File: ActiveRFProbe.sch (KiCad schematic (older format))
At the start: 41 parts, among them J1 Conn_01x01, J16 Conn_01x01, J17 Conn_01x01, J18 Conn_01x01, J19 Conn_01x01, J2 Conn_01x01, J20 Conn_01x01, J21 Conn_01x01, J22 Conn_01x01, J23 Conn_01x01, J24 Conn_01x01, J25 Conn_Coaxial, J3 Conn_01x01, Q1 2SC3357, Q2 2SC3357, Q3 2SC3357

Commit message: Fixed edge detector
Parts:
- removed C7: 10 nF, Capacitors_SMD:C_0805_HandSoldering, symbol C_Small
- added R13: 10k, Resistors_SMD:R_0805_HandSoldering, symbol R
- J25: footprint ActiveRFProbe:bnc_90_1-1337543-0_pad_combo -> ActiveRFProbe:Amphenol_RF_SMA_132289
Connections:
- net GND: now also R13.1
- net at C6.2, Q3.1 (E), R10.1: now also R9.2
- net at C8.2, D5.1 (K), J17.1 (Pin_1): now also R13.2
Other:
- moved on the sheet: D5, R9
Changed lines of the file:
@@
 L R R9
 U 1 1 5E9BA4DA
-P 6050 4450
-F 0 "R9" V 6130 4450 50  0000 C CNN
-F 1 "10k" V 6050 4450 50  0000 C CNN
-F 2 "Resistors_SMD:R_0805_HandSoldering" V 5980 4450 50  0001 C CNN
-F 3 "" H 6050 4450 50  0001 C CNN
-	1    6050 4450
+P 5850 4450
+F 0 "R9" V 5930 4450 50  0000 C CNN
+F 1 "10k" V 5850 4450 50  0000 C CNN
+F 2 "Resistors_SMD:R_0805_HandSoldering" V 5780 4450 50  0001 C CNN
+F 3 "" H 5850 4450 50  0001 C CNN
+	1    5850 4450
 	0    1    1    0
 $EndComp
@@
 $EndComp
 $Comp
-L C_Small C7
-U 1 1 5E9DAA86
-P 5800 4450
-F 0 "C7" H 5810 4520 50  0000 L CNN
-F 1 "10 nF" V 5650 4350 50  0000 L CNN
-F 2 "Capacitors_SMD:C_0805_HandSoldering" H 5800 4450 50  0001 C CNN
-F 3 "" H 5800 4450 50  0001 C CNN
-	1    5800 4450
-	0    1    1    0
-$EndComp
-$Comp
-L GND #PWR17
+L GND #PWR18
 U 1 1 5E9DC195
 P 6750 4950
-F 0 "#PWR17" H 6750 4700 50  0001 C CNN
+F 0 "#PWR18" H 6750 4700 50  0001 C CNN
 F 1 "GND" H 6750 4800 50  0000 C CNN
 F 2 "" H 6750 4950 50  0001 C CNN
@@
 F 0 "J25" H 6460 3870 50  0000 C CNN
 F 1 "Conn_Coaxial" V 6565 3750 50  0000 C CNN
-F 2 "ActiveRFProbe:bnc_90_1-1337543-0_pad_combo" H 6450 3750 50  0001 C CNN
+F 2 "ActiveRFProbe:Amphenol_RF_SMA_132289" H 6450 3750 50  0001 C CNN
 F 3 "" H 6450 3750 50  0001 C CNN
 	1    6450 3750
@@
 L D_Schottky D5
 U 1 1 5E9C8115
-P 6450 4450
-F 0 "D5" H 6450 4550 50  0000 C CNN
-F 1 "LRB751V" H 6450 4350 50  0000 C CNN
-F 2 "Diodes_SMD:D_SOD-323_HandSoldering" H 6450 4450 50  0001 C CNN
-F 3 "" H 6450 4450 50  0001 C CNN
-	1    6450 4450
-	-1   0    0    1
-$EndComp
-$Comp
-L GND #PWR18
+P 6200 4450
+F 0 "D5" H 6200 4550 50  0000 C CNN
+F 1 "LRB751V" H 6200 4350 50  0000 C CNN
+F 2 "Diodes_SMD:D_SOD-323_HandSoldering" H 6200 4450 50  0001 C CNN
+F 3 "" H 6200 4450 50  0001 C CNN
+	1    6200 4450
+	-1   0    0    1
+$EndComp
+$Comp
+L GND #PWR19
 U 1 1 5E9E423A
 P 7150 4950
-F 0 "#PWR18" H 7150 4700 50  0001 C CNN
+F 0 "#PWR19" H 7150 4700 50  0001 C CNN
 F 1 "GND" H 7150 4800 50  0000 C CNN
 F 2 "" H 7150 4950 50  0001 C CNN
@@
 Connection ~ 5700 4250
 Wire Wire Line
-	5900 4450 5900 4450
-Wire Wire Line
-	6600 4450 7150 4450
+	6350 4450 7150 4450
 Wire Wire Line
 	6750 4950 6750 4750
@@
 Wire Wire Line
 	3500 1800 3500 1900
-Wire Wire Line
-	6300 4450 6200 4450
 Wire Wire Line
 	7150 4950 7150 4700
@@
 	1    0    0    -1
 $EndComp
+$Comp
+L R R13
+U 1 1 5E9E674D
+P 6450 4650
+F 0 "R13" V 6530 4650 50  0000 C CNN
+F 1 "10k" V 6450 4650 50  0000 C CNN
+F 2 "Resistors_SMD:R_0805_HandSoldering" V 6380 4650 50  0001 C CNN
+F 3 "" H 6450 4650 50  0001 C CNN
+	1    6450 4650
+	-1   0    0    1
+$EndComp
+Wire Wire Line
+	6450 4500 6450 4450
+Connection ~ 6450 4450
+$Comp
+L GND #PWR17
+U 1 1 5E9E68D7
+P 6450 4950
+F 0 "#PWR17" H 6450 4700 50  0001 C CNN
+F 1 "GND" H 6450 4800 50  0000 C CNN
+F 2 "" H 6450 4950 50  0001 C CNN
+F 3 "" H 6450 4950 50  0001 C CNN
+	1    6450 4950
+	1    0    0    -1
+$EndComp
+Wire Wire Line
+	6450 4950 6450 4800
+Wire Wire Line
+	6050 4450 6000 4450
 $EndSCHEMATC

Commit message: Cleaned up the layout
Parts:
- removed R1, R3: 10k, Resistors_SMD:R_0805_HandSoldering, symbol R
- removed R7, R8: 1k, Resistors_SMD:R_0805_HandSoldering, symbol R
- R11: value 10k -> 47k
- R12: value 1k -> 47k
- R4: value 22k -> 10k
- R5: value 0R -> 22R
- R6: value 220R -> 100R
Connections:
- net +9V: now also C16.2, D6.2 (A), J2.1 (Pin_1), R11.2, R12.2
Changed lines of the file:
@@
 $EndDescr
-$Comp
-L R R1
-U 1 1 5E9B8F5B
-P 3050 3400
-F 0 "R1" V 3130 3400 50  0000 C CNN
-F 1 "10k" V 3050 3400 50  0000 C CNN
-F 2 "Resistors_SMD:R_0805_HandSoldering" V 2980 3400 50  0001 C CNN
-F 3 "" H 3050 3400 50  0001 C CNN
-	1    3050 3400
-	0    1    1    0
-$EndComp
 $Comp
 L C_Small C1
@@
 $EndComp
 $Comp
-L GND #PWR6
+L GND #PWR01
 U 1 1 5E9B90E6
 P 3200 4600
-F 0 "#PWR6" H 3200 4350 50  0001 C CNN
+F 0 "#PWR01" H 3200 4350 50  0001 C CNN
 F 1 "GND" H 3200 4450 50  0000 C CNN
 F 2 "" H 3200 4600 50  0001 C CNN
@@
 	1    3200 4350
 	1    0    0    -1
-$EndComp
-$Comp
-L R R3
-U 1 1 5E9B91B8
-P 2650 3400
-F 0 "R3" V 2730 3400 50  0000 C CNN
-F 1 "10k" V 2650 3400 50  0000 C CNN
-F 2 "Resistors_SMD:R_0805_HandSoldering" V 2580 3400 50  0001 C CNN
-F 3 "" H 2650 3400 50  0001 C CNN
-	1    2650 3400
-	0    1    1    0
 $EndComp
 $Comp
@@
 $EndComp
 $Comp
-L GND #PWR11
+L GND #PWR02
 U 1 1 5E9B935A
 P 4550 4750
-F 0 "#PWR11" H 4550 4500 50  0001 C CNN
+F 0 "#PWR02" H 4550 4500 50  0001 C CNN
 F 1 "GND" H 4550 4600 50  0000 C CNN
 F 2 "" H 4550 4750 50  0001 C CNN
@@
 P 4150 4000
 F 0 "R4" V 4230 4000 50  0000 C CNN
-F 1 "22k" V 4150 4000 50  0000 C CNN
+F 1 "10k" V 4150 4000 50  0000 C CNN
 F 2 "Resistors_SMD:R_0805_HandSoldering" V 4080 4000 50  0001 C CNN
 F 3 "" H 4150 4000 50  0001 C CNN
@@
 P 4550 3650
 F 0 "R6" V 4630 3650 50  0000 C CNN
-F 1 "220R" V 4550 3650 50  0000 C CNN
+F 1 "100R" V 4550 3650 50  0000 C CNN
 F 2 "Resistors_SMD:R_0805_HandSoldering" V 4480 3650 50  0001 C CNN
 F 3 "" H 4550 3650 50  0001 C CNN
@@
 P 4550 4550
 F 0 "R5" V 4630 4550 50  0000 C CNN
-F 1 "0R" V 4550 4550 50  0000 C CNN
+F 1 "22R" V 4550 4550 50  0000 C CNN
 F 2 "Resistors_SMD:R_0805_HandSoldering" V 4480 4550 50  0001 C CNN
 F 3 "" H 4550 4550 50  0001 C CNN
 	1    4550 4550
 	-1   0    0    1
-$EndComp
-$Comp
-L R R7
-U 1 1 5E9B9913
-P 5300 3350
-F 0 "R7" V 5380 3350 50  0000 C CNN
-F 1 "1k" V 5300 3350 50  0000 C CNN
-F 2 "Resistors_SMD:R_0805_HandSoldering" V 5230 3350 50  0001 C CNN
-F 3 "" H 5300 3350 50  0001 C CNN
-	1    5300 3350
-	0    1    1    0
 $EndComp
 $Comp
@@
 $EndComp
 $Comp
-L R R8
-U 1 1 5E9B9DF6
-P 4850 3350
-F 0 "R8" V 4930 3350 50  0000 C CNN
-F 1 "1k" V 4850 3350 50  0000 C CNN
-F 2 "Resistors_SMD:R_0805_HandSoldering" V 4780 3350 50  0001 C CNN
-F 3 "" H 4850 3350 50  0001 C CNN
-	1    4850 3350
-	0    1    1    0
-$EndComp
-$Comp
 L C_Small C6
 U 1 1 5E9B9FF2
@@
 $EndComp
 $Comp
-L GND #PWR4
+L GND #PWR03
 U 1 1 5E9C1122
 P 3100 2550
-F 0 "#PWR4" H 3100 2300 50  0001 C CNN
+F 0 "#PWR03" H 3100 2300 50  0001 C CNN
 F 1 "GND" H 3100 2400 50  0000 C CNN
 F 2 "" H 3100 2550 50  0001 C CNN
@@
 $EndComp
 $Comp
-L GND #PWR2
+L GND #PWR04
 U 1 1 5E9C57D4
 P 2350 3550
-F 0 "#PWR2" H 2350 3300 50  0001 C CNN
+F 0 "#PWR04" H 2350 3300 50  0001 C CNN
 F 1 "GND" H 2350 3400 50  0000 C CNN
 F 2 "" H 2350 3550 50  0001 C CNN
@@
 $EndComp
 $Comp
-L +9V #PWR3
+L +9V #PWR05
 U 1 1 5E9C9102
 P 3100 1500
-F 0 "#PWR3" H 3100 1350 50  0001 C CNN
+F 0 "#PWR05" H 3100 1350 50  0001 C CNN
 F 1 "+9V" H 3100 1640 50  0000 C CNN
 F 2 "" H 3100 1500 50  0001 C CNN
@@
 $EndComp
 $Comp
-L GND #PWR1
+L GND #PWR06
 U 1 1 5E9CFF23
 P 2200 2500
-F 0 "#PWR1" H 2200 2250 50  0001 C CNN
+F 0 "#PWR06" H 2200 2250 50  0001 C CNN
 F 1 "GND" H 2200 2350 50  0000 C CNN
 F 2 "" H 2200 2500 50  0001 C CNN
@@
 $EndComp
 $Comp
-L +9V #PWR5
+L +9V #PWR07
 U 1 1 5E9D5F5F
 P 3200 3250
-F 0 "#PWR5" H 3200 3100 50  0001 C CNN
+F 0 "#PWR07" H 3200 3100 50  0001 C CNN
 F 1 "+9V" H 3200 3390 50  0000 C CNN
 F 2 "" H 3200 3250 50  0001 C CNN
@@
 $EndComp
 $Comp
-L GND #PWR8
+L GND #PWR08
 U 1 1 5E9D6577
 P 3550 3550
-F 0 "#PWR8" H 3550 3300 50  0001 C CNN
+F 0 "#PWR08" H 3550 3300 50  0001 C CNN
 F 1 "GND" H 3550 3400 50  0000 C CNN
 F 2 "" H 3550 3550 50  0001 C CNN
@@
 $EndComp
 $Comp
-L +9V #PWR10
+L +9V #PWR09
 U 1 1 5E9D7A25
 P 4550 3200
-F 0 "#PWR10" H 4550 3050 50  0001 C CNN
+F 0 "#PWR09" H 4550 3050 50  0001 C CNN
 F 1 "+9V" H 4550 3340 50  0000 C CNN
 F 2 "" H 4550 3200 50  0001 C CNN
@@
 $EndComp
 $Comp
-L GND #PWR9
+L GND #PWR010
 U 1 1 5E9D80F3
 P 4250 3500
-F 0 "#PWR9" H 4250 3250 50  0001 C CNN
+F 0 "#PWR010" H 4250 3250 50  0001 C CNN
 F 1 "GND" H 4250 3350 50  0000 C CNN
 F 2 "" H 4250 3500 50  0001 C CNN
@@
 $EndComp
 $Comp
-L GND #PWR14
+L GND #PWR011
 U 1 1 5E9D96E5
 P 5500 4800
-F 0 "#PWR14" H 5500 4550 50  0001 C CNN
+F 0 "#PWR011" H 5500 4550 50  0001 C CNN
 F 1 "GND" H 5500 4650 50  0000 C CNN
 F 2 "" H 5500 4800 50  0001 C CNN
@@
 $EndComp
 $Comp
-L +9V #PWR13
+L +9V #PWR012
 U 1 1 5E9DA181
 P 5500 3200
-F 0 "#PWR13" H 5500 3050 50  0001 C CNN
+F 0 "#PWR012" H 5500 3050 50  0001 C CNN
 F 1 "+9V" H 5500 3340 50  0000 C CNN
 F 2 "" H 5500 3200 50  0001 C CNN
@@
 $EndComp
 $Comp
-L GND #PWR15
+L GND #PWR013
 U 1 1 5E9DA538
 P 5850 3450
-F 0 "#PWR15" H 5850 3200 50  0001 C CNN
+F 0 "#PWR013" H 5850 3200 50  0001 C CNN
 F 1 "GND" H 5850 3300 50  0000 C CNN
 F 2 "" H 5850 3450 50  0001 C CNN
@@
 $EndComp
 $Comp
-L GND #PWR18
+L GND #PWR014
 U 1 1 5E9DC195
 P 6750 4950
-F 0 "#PWR18" H 6750 4700 50  0001 C CNN
+F 0 "#PWR014" H 6750 4700 50  0001 C CNN
 F 1 "GND" H 6750 4800 50  0000 C CNN
 F 2 "" H 6750 4950 50  0001 C CNN
@@
 $EndComp
 $Comp
-L GND #PWR16
+L GND #PWR015
 U 1 1 5E9DE267
 P 6450 4200
-F 0 "#PWR16" H 6450 3950 50  0001 C CNN
+F 0 "#PWR015" H 6450 3950 50  0001 C CNN
 F 1 "GND" H 6450 4050 50  0000 C CNN
 F 2 "" H 6450 4200 50  0001 C CNN
@@
 $EndComp
 $Comp
-L GND #PWR7
+L GND #PWR016
 U 1 1 5E9DEDB9
 P 3500 1900
-F 0 "#PWR7" H 3500 1650 50  0001 C CNN
+F 0 "#PWR016" H 3500 1650 50  0001 C CNN
 F 1 "GND" H 3500 1750 50  0000 C CNN
 F 2 "" H 3500 1900 50  0001 C CNN
@@
 $EndComp
 $Comp
-L GND #PWR19
+L GND #PWR017
 U 1 1 5E9E423A
 P 7150 4950
-F 0 "#PWR19" H 7150 4700 50  0001 C CNN
+F 0 "#PWR017" H 7150 4700 50  0001 C CNN
 F 1 "GND" H 7150 4800 50  0000 C CNN
 F 2 "" H 7150 4950 50  0001 C CNN
@@
 	3100 2300 3200 2300
 Wire Wire Line
-	2350 3400 2350 3550
+	2350 3450 2350 3550
 Wire Wire Line
 	2350 3450 2300 3450
@@
 Wire Wire Line
 	5500 3200 5500 3650
-Wire Wire Line
-	5450 3350 5600 3350
 Connection ~ 5500 3350
 Wire Wire Line
@@
 	3100 2300 3100 2100
 Wire Wire Line
-	3100 1800 3100 1550
+	3100 1500 3100 1800
 Wire Wire Line
 	4550 4700 4550 4750
@@
 	2500 3900 2300 3900
 Wire Wire Line
-	2800 3400 2900 3400
-Connection ~ 2850 3400
-Wire Wire Line
-	2500 3400 2350 3400
-Connection ~ 2350 3450
+	2850 3400 3300 3400
 $Comp
 L R R11
@@
 P 2850 3650
 F 0 "R11" V 2930 3650 50  0000 C CNN
-F 1 "10k" V 2850 3650 50  0000 C CNN
+F 1 "47k" V 2850 3650 50  0000 C CNN
 F 2 "Resistors_SMD:R_0805_HandSoldering" V 2780 3650 50  0001 C CNN
 F 3 "" H 2850 3650 50  0001 C CNN
@@
 	-1   0    0    1
 $EndComp
-$Comp
-L GND #PWR12
-U 1 1 5E9D43F0
-P 4700 3400
-F 0 "#PWR12" H 4700 3150 50  0001 C CNN
-F 1 "GND" H 4700 3250 50  0000 C CNN
-F 2 "" H 4700 3400 50  0001 C CNN
-F 3 "" H 4700 3400 50  0001 C CNN
-	1    4700 3400
-	1    0    0    -1
-$EndComp
-Wire Wire Line
-	4700 3400 4700 3350
-Wire Wire Line
-	5000 3350 5150 3350
-Connection ~ 5050 3350
-Wire Wire Line
-	3300 3400 3200 3400
 $Comp
 L R R12
@@
 P 5050 3600
 F 0 "R12" V 5130 3600 50  0000 C CNN
-F 1 "1k" V 5050 3600 50  0000 C CNN
+F 1 "47k" V 5050 3600 50  0000 C CNN
 F 2 "Resistors_SMD:R_0805_HandSoldering" V 4980 3600 50  0001 C CNN
 F 3 "" H 5050 3600 50  0001 C CNN
@@
 Connection ~ 6450 4450
 $Comp
-L GND #PWR17
+L GND #PWR018
 U 1 1 5E9E68D7
 P 6450 4950
-F 0 "#PWR17" H 6450 4700 50  0001 C CNN
+F 0 "#PWR018" H 6450 4700 50  0001 C CNN
 F 1 "GND" H 6450 4800 50  0000 C CNN
 F 2 "" H 6450 4950 50  0001 C CNN
@@
 Wire Wire Line
 	6050 4450 6000 4450
+Wire Wire Line
+	5050 3350 5600 3350
 $EndSCHEMATC

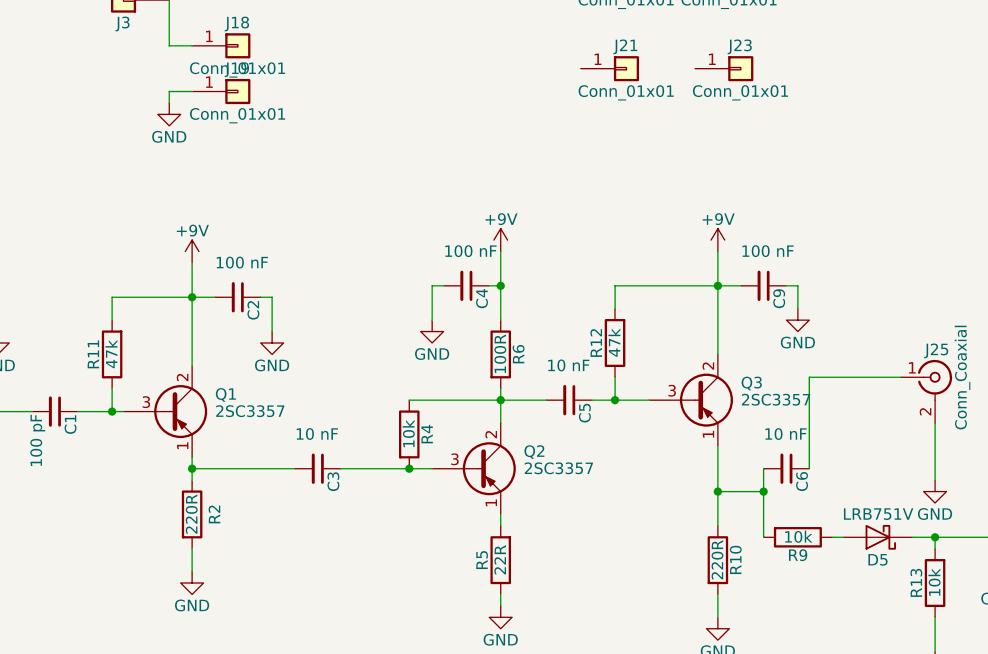
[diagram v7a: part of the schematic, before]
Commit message: Added LCSC parts, fixed symbol, added decoupling resistors
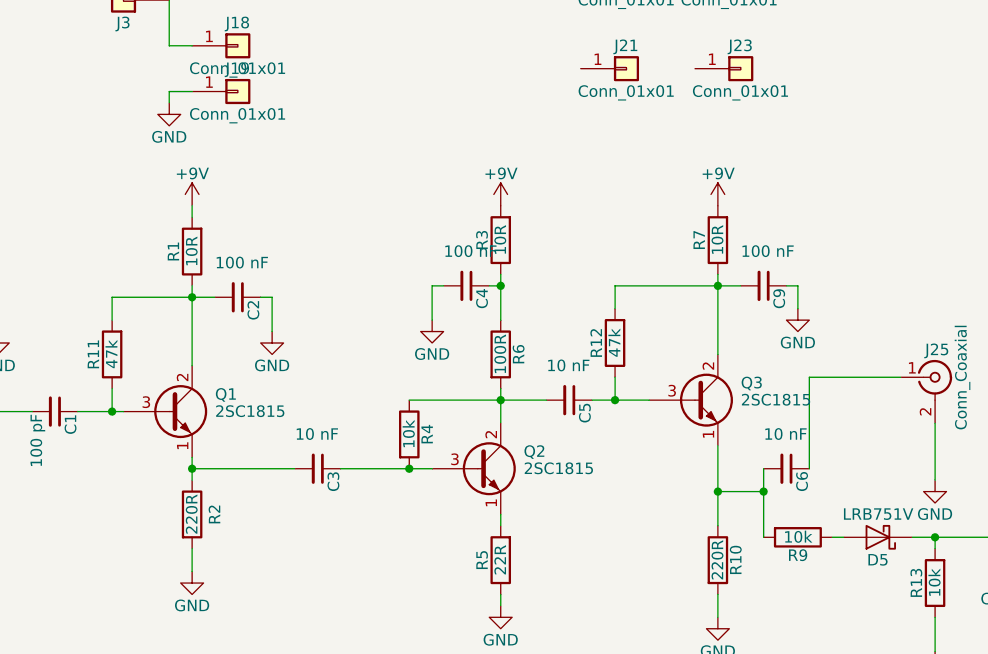
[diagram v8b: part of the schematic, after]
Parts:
- removed Q1, Q2, Q3: 2SC3357, TO_SOT_Packages_SMD:SOT-89-3_Handsoldering, symbol 2SA1015
- added Q1, Q2, Q3: 2SC1815, TO_SOT_Packages_SMD:SOT-89-3_Handsoldering, symbol 2SC1815
- added R1, R3, R7: 10R, Resistors_SMD:R_0805_HandSoldering, symbol R
- C1: LCSC (none) -> C1790
- C16: footprint Capacitors_SMD:C_1210_HandSoldering -> Capacitors_SMD:C_0805_HandSoldering; LCSC (none) -> C45783
- C2, C4, C9: LCSC (none) -> C49678
- C3, C5, C6, C8: LCSC (none) -> C1710
- D5: LCSC (none) -> C131730
- D6: LCSC (none) -> C2296
- R10, R2: LCSC (none) -> C17557
- R11, R12: LCSC (none) -> C17713
- R13, R4, R9: LCSC (none) -> C17414
- R14: LCSC (none) -> C17513
- R5: LCSC (none) -> C17561
- R6: LCSC (none) -> C17408
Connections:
- net +9V: now also R1.2, R3.2, R7.2; no longer C2.2, C4.1, C9.2, R11.2, R12.2, R6.1
- net at C1.1, R11.1: now also Q1.3 (B)
- net at C3.2, R2.1: now also Q1.1 (E)
- net at C3.1, R4.2: now also Q2.3 (B)
- net at C5.2, R4.1, R6.2: now also Q2.2 (C)
- net at R5.2: now also Q2.1 (E)
- net at C5.1, R12.1: now also Q3.3 (B)
- net at C6.2, R10.1, R9.2: now also Q3.1 (E)
- new net: C4.1, R3.1, R6.1
- new net: C2.2, Q1.2 (C), R1.1, R11.2
- new net: C9.2, Q3.2 (C), R12.2, R7.1
